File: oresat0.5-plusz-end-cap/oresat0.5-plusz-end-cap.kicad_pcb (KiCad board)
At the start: 2 copper layers, 105.6 x 105.6 mm, 44 parts, among them J2 U.FL-R-SMA, U1 LTC4305, U2 MMC5883MA, U3 MMC5883MA

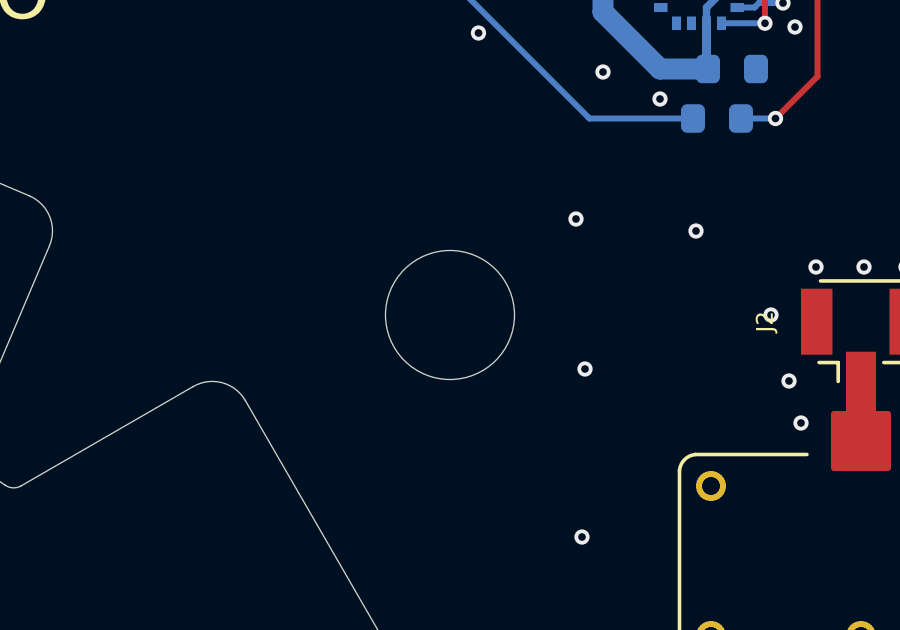
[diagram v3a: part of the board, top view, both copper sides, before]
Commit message: Oresat0.5 +Z End Cap. Still some weird library issues, but skipping for now.
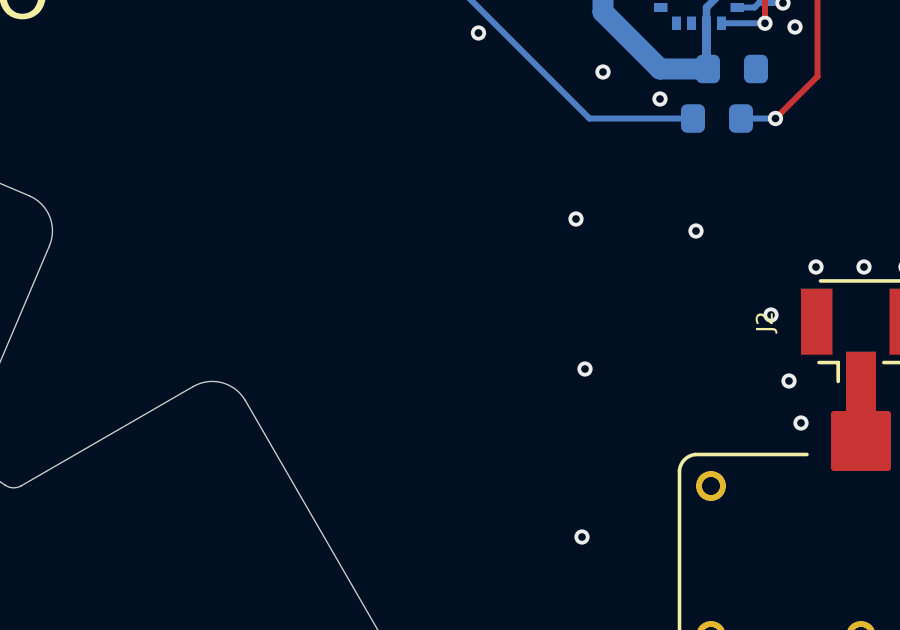
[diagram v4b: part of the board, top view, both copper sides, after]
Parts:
- removed REF**: MountingHole_4.3mm_M4, MountingHole:MountingHole_4.3mm_M4
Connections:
- U2 pad 12: (no net) -> unconnected-(U2-NC-Pad12)
- U2 pad 14: (no net) -> unconnected-(U2-NC-Pad14)
- U2 pad 3: (no net) -> unconnected-(U2-NC-Pad3)
- U2 pad 4: (no net) -> unconnected-(U2-NC-Pad4)
- U2 pad 5: (no net) -> unconnected-(U2-NC-Pad5)
- U2 pad 6: (no net) -> unconnected-(U2-NC-Pad6)
- U2 pad 7: (no net) -> unconnected-(U2-NC-Pad7)
- U2 pad 8: (no net) -> unconnected-(U2-NC-Pad8)
- U3 pad 12: (no net) -> unconnected-(U3-NC-Pad12)
- U3 pad 14: (no net) -> unconnected-(U3-NC-Pad14)
- U3 pad 3: (no net) -> unconnected-(U3-NC-Pad3)
- U3 pad 4: (no net) -> unconnected-(U3-NC-Pad4)
- U3 pad 5: (no net) -> unconnected-(U3-NC-Pad5)
- U3 pad 6: (no net) -> unconnected-(U3-NC-Pad6)
- U3 pad 7: (no net) -> unconnected-(U3-NC-Pad7)
- U3 pad 8: (no net) -> unconnected-(U3-NC-Pad8)
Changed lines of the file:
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@@
     (pad_to_mask_clearance 0)
     (pcbplotparams
-      (layerselection 0x0001000_7ffffffe)
+      (layerselection 0x00010fc_ffffffff)
       (plot_on_all_layers_selection 0x0000000_00000000)
       (disableapertmacros false)
@@
       (usegerberattributes true)
       (usegerberadvancedattributes true)
-      (creategerberjobfile true)
+      (creategerberjobfile false)
       (dashed_line_dash_ratio 12.000000)
       (dashed_line_gap_ratio 3.000000)
@@
       (drillshape 0)
       (scaleselection 1)
-      (outputdirectory "")
+      (outputdirectory "build")
     )
   )
@@
   (net 22 "unconnected-(J1-Pad12)")
   (net 23 "Net-(U2-INT)")
+  (net 24 "unconnected-(U2-NC-Pad3)")
+  (net 25 "unconnected-(U2-NC-Pad4)")
+  (net 26 "unconnected-(U2-NC-Pad5)")
+  (net 27 "unconnected-(U2-NC-Pad6)")
+  (net 28 "unconnected-(U2-NC-Pad7)")
+  (net 29 "unconnected-(U2-NC-Pad8)")
+  (net 30 "unconnected-(U2-NC-Pad12)")
+  (net 31 "unconnected-(U2-NC-Pad14)")
+  (net 32 "unconnected-(U3-NC-Pad3)")
+  (net 33 "unconnected-(U3-NC-Pad4)")
+  (net 34 "unconnected-(U3-NC-Pad5)")
+  (net 35 "unconnected-(U3-NC-Pad6)")
+  (net 36 "unconnected-(U3-NC-Pad7)")
+  (net 37 "unconnected-(U3-NC-Pad8)")
+  (net 38 "unconnected-(U3-NC-Pad12)")
+  (net 39 "unconnected-(U3-NC-Pad14)")
   (footprint "Connector_Coaxial:U.FL_Hirose_U.FL-R-SMT-1_Vertical" (layer "F.Cu")
     (at 191.9 78.7 90)
@@
       (net 6 "/MAG-SDA") (pinfunction "1") (pintype "passive"))
   )
-  (footprint "MountingHole:MountingHole_4.3mm_M4" (layer "F.Cu")
-    (at 178.2 78)
-    (descr "Mounting Hole 4.3mm, no annular, M4")
-    (tags "mounting hole 4.3mm no annular m4")
-    (attr exclude_from_pos_files exclude_from_bom)
-    (fp_text reference "REF**" (at 0 -5.3) (layer "F.SilkS") hide
-        (effects (font (size 0.56 0.56) (thickness 0.12)))
-    )
-    (fp_text value "MountingHole_4.3mm_M4" (at 0 5.3) (layer "F.Fab")
-        (effects (font (size 1 1) (thickness 0.15)))
-    )
-    (fp_text user "${REFERENCE}" (at 0 0) (layer "F.Fab")
-        (effects (font (size 1 1) (thickness 0.15)))
-    )
-    (fp_circle (center 0 0) (end 4.3 0)
-      (stroke (width 0.15) (type solid)) (fill none) (layer "Cmts.User"))
-    (fp_circle (center 0 0) (end 4.55 0)
-      (stroke (width 0.05) (type solid)) (fill none) (layer "F.CrtYd"))
-    (pad "" np_thru_hole circle (at 0 0) (size 4.3 4.3) (drill 4.3) (layers "*.Cu" "*.Mask"))
-  )
   (footprint "MountingHole:MountingHole_2.1mm" (layer "F.Cu")
     (at 121 154.5)
@@
       (net 1 "3.3V") (pinfunction "VDD") (pintype "power_in") (solder_mask_margin 0.0635))
     (pad "3" smd rect (at -0.25 1.275 90) (size 0.3 0.45) (layers "B.Cu" "B.Paste" "B.Mask")
-      (pinfunction "NC") (pintype "no_connect") (solder_mask_margin 0.0635))
+      (net 32 "unconnected-(U3-NC-Pad3)") (pinfunction "NC") (pintype "no_connect") (solder_mask_margin 0.0635))
     (pad "4" smd rect (at -0.75 1.275 90) (size 0.3 0.45) (layers "B.Cu" "B.Paste" "B.Mask")
-      (pinfunction "NC") (pintype "no_connect") (solder_mask_margin 0.0635))
+      (net 33 "unconnected-(U3-NC-Pad4)") (pinfunction "NC") (pintype "no_connect") (solder_mask_margin 0.0635))
     (pad "5" smd rect (at -1.275 0.75) (size 0.3 0.45) (layers "B.Cu" "B.Paste" "B.Mask")
-      (pinfunction "NC") (pintype "no_connect") (solder_mask_margin 0.0635))
+      (net 34 "unconnected-(U3-NC-Pad5)") (pinfunction "NC") (pintype "no_connect") (solder_mask_margin 0.0635))
     (pad "6" smd rect (at -1.275 0.25) (size 0.3 0.45) (layers "B.Cu" "B.Paste" "B.Mask")
-      (pinfunction "NC") (pintype "no_connect") (solder_mask_margin 0.0635))
+      (net 35 "unconnected-(U3-NC-Pad6)") (pinfunction "NC") (pintype "no_connect") (solder_mask_margin 0.0635))
     (pad "7" smd rect (at -1.275 -0.25) (size 0.3 0.45) (layers "B.Cu" "B.Paste" "B.Mask")
-      (pinfunction "NC") (pintype "no_connect") (solder_mask_margin 0.0635))
+      (net 36 "unconnected-(U3-NC-Pad7)") (pinfunction "NC") (pintype "no_connect") (solder_mask_margin 0.0635))
     (pad "8" smd rect (at -1.275 -0.75) (size 0.3 0.45) (layers "B.Cu" "B.Paste" "B.Mask")
-      (pinfunction "NC") (pintype "no_connect") (solder_mask_margin 0.0635))
+      (net 37 "unconnected-(U3-NC-Pad8)") (pinfunction "NC") (pintype "no_connect") (solder_mask_margin 0.0635))
     (pad "9" smd rect (at -0.75 -1.275 270) (size 0.3 0.45) (layers "B.Cu" "B.Paste" "B.Mask")
       (net 2 "GND") (pinfunction "GND") (pintype "power_in") (solder_mask_margin 0.0635))
@@
       (net 2 "GND") (pinfunction "GND") (pintype "power_in") (solder_mask_margin 0.0635))
     (pad "12" smd rect (at 0.75 -1.275 270) (size 0.3 0.45) (layers "B.Cu" "B.Paste" "B.Mask")
-      (pinfunction "NC") (pintype "no_connect") (solder_mask_margin 0.0635))
+      (net 38 "unconnected-(U3-NC-Pad12)") (pinfunction "NC") (pintype "no_connect") (solder_mask_margin 0.0635))
     (pad "13" smd rect (at 1.275 -0.75 180) (size 0.3 0.45) (layers "B.Cu" "B.Paste" "B.Mask")
       (net 1 "3.3V") (pinfunction "VDDIO") (pintype "power_in") (solder_mask_margin 0.0635))
     (pad "14" smd rect (at 1.275 -0.25 180) (size 0.3 0.45) (layers "B.Cu" "B.Paste" "B.Mask")
-      (pinfunction "NC") (pintype "no_connect") (solder_mask_margin 0.0635))
+      (net 39 "unconnected-(U3-NC-Pad14)") (pinfunction "NC") (pintype "no_connect") (solder_mask_margin 0.0635))
     (pad "15" smd rect (at 1.275 0.25 180) (size 0.3 0.45) (layers "B.Cu" "B.Paste" "B.Mask")
       (net 21 "Net-(U3-INT)") (pinfunction "INT") (pintype "output") (solder_mask_margin 0.0635))
@@
       (net 1 "3.3V") (pinfunction "VDD") (pintype "power_in") (solder_mask_margin 0.0635))
     (pad "3" smd rect (at -0.25 1.275) (size 0.3 0.45) (layers "B.Cu" "B.Paste" "B.Mask")
-      (pinfunction "NC") (pintype "no_connect") (solder_mask_margin 0.0635))
+      (net 24 "unconnected-(U2-NC-Pad3)") (pinfunction "NC") (pintype "no_connect") (solder_mask_margin 0.0635))
     (pad "4" smd rect (at -0.75 1.275) (size 0.3 0.45) (layers "B.Cu" "B.Paste" "B.Mask")
-      (pinfunction "NC") (pintype "no_connect") (solder_mask_margin 0.0635))
+      (net 25 "unconnected-(U2-NC-Pad4)") (pinfunction "NC") (pintype "no_connect") (solder_mask_margin 0.0635))
     (pad "5" smd rect (at -1.275 0.75 270) (size 0.3 0.45) (layers "B.Cu" "B.Paste" "B.Mask")
-      (pinfunction "NC") (pintype "no_connect") (solder_mask_margin 0.0635))
+      (net 26 "unconnected-(U2-NC-Pad5)") (pinfunction "NC") (pintype "no_connect") (solder_mask_margin 0.0635))
     (pad "6" smd rect (at -1.275 0.25 270) (size 0.3 0.45) (layers "B.Cu" "B.Paste" "B.Mask")
-      (pinfunction "NC") (pintype "no_connect") (solder_mask_margin 0.0635))
+      (net 27 "unconnected-(U2-NC-Pad6)") (pinfunction "NC") (pintype "no_connect") (solder_mask_margin 0.0635))
     (pad "7" smd rect (at -1.275 -0.25 270) (size 0.3 0.45) (layers "B.Cu" "B.Paste" "B.Mask")
-      (pinfunction "NC") (pintype "no_connect") (solder_mask_margin 0.0635))
+      (net 28 "unconnected-(U2-NC-Pad7)") (pinfunction "NC") (pintype "no_connect") (solder_mask_margin 0.0635))
     (pad "8" smd rect (at -1.275 -0.75 270) (size 0.3 0.45) (layers "B.Cu" "B.Paste" "B.Mask")
-      (pinfunction "NC") (pintype "no_connect") (solder_mask_margin 0.0635))
+      (net 29 "unconnected-(U2-NC-Pad8)") (pinfunction "NC") (pintype "no_connect") (solder_mask_margin 0.0635))
     (pad "9" smd rect (at -0.75 -1.275 180) (size 0.3 0.45) (layers "B.Cu" "B.Paste" "B.Mask")
       (net 2 "GND") (pinfunction "GND") (pintype "power_in") (solder_mask_margin 0.0635))
@@
       (net 2 "GND") (pinfunction "GND") (pintype "power_in") (solder_mask_margin 0.0635))
     (pad "12" smd rect (at 0.75 -1.275 180) (size 0.3 0.45) (layers "B.Cu" "B.Paste" "B.Mask")
-      (pinfunction "NC") (pintype "no_connect") (solder_mask_margin 0.0635))
+      (net 30 "unconnected-(U2-NC-Pad12)") (pinfunction "NC") (pintype "no_connect") (solder_mask_margin 0.0635))
     (pad "13" smd rect (at 1.275 -0.75 90) (size 0.3 0.45) (layers "B.Cu" "B.Paste" "B.Mask")
       (net 1 "3.3V") (pinfunction "VDDIO") (pintype "power_in") (solder_mask_margin 0.0635))
     (pad "14" smd rect (at 1.275 -0.25 90) (size 0.3 0.45) (layers "B.Cu" "B.Paste" "B.Mask")
-      (pinfunction "NC") (pintype "no_connect") (solder_mask_margin 0.0635))
+      (net 31 "unconnected-(U2-NC-Pad14)") (pinfunction "NC") (pintype "no_connect") (solder_mask_margin 0.0635))
     (pad "15" smd rect (at 1.275 0.25 90) (size 0.3 0.45) (layers "B.Cu" "B.Paste" "B.Mask")
       (net 23 "Net-(U2-INT)") (pinfunction "INT") (pintype "output") (solder_mask_margin 0.0635))

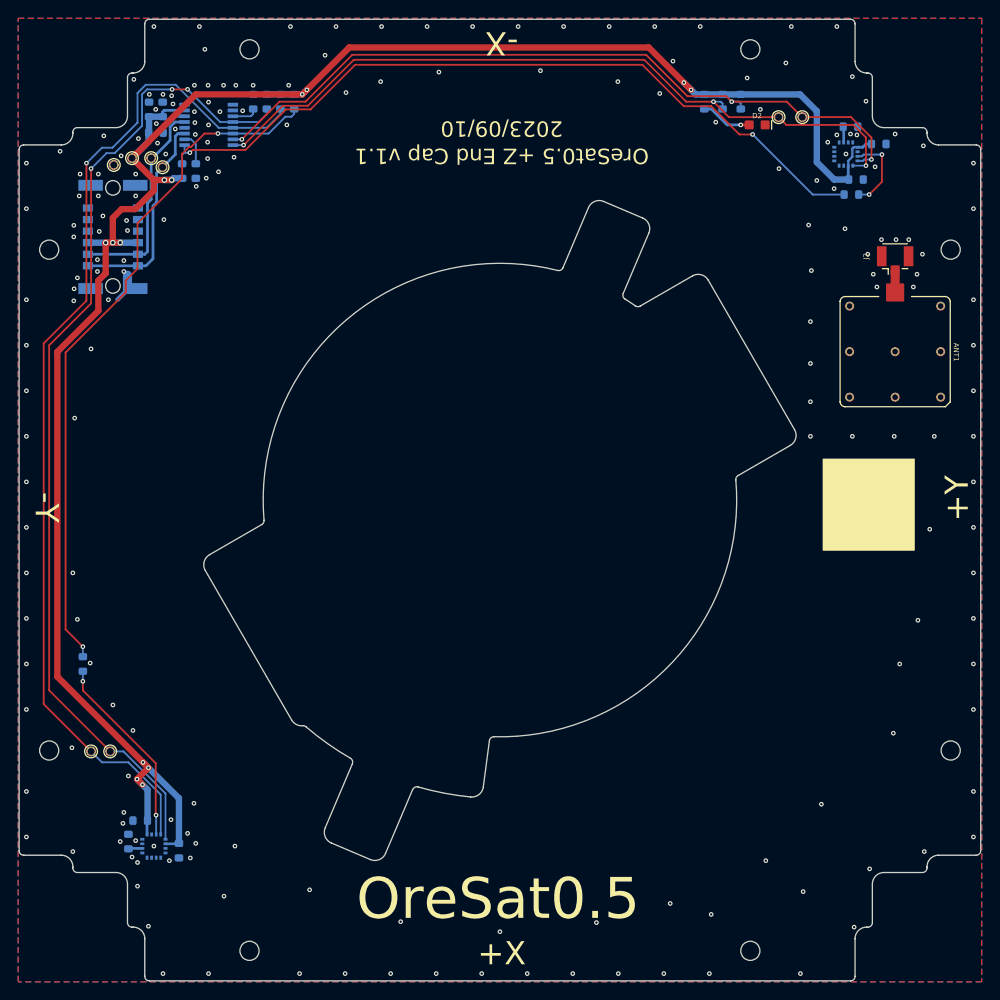
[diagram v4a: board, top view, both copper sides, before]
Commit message: Upgrades OreSat0.5 +Z End Cap to v1.2 -- fits the new deployer, and cleans up a bunch of library issues.
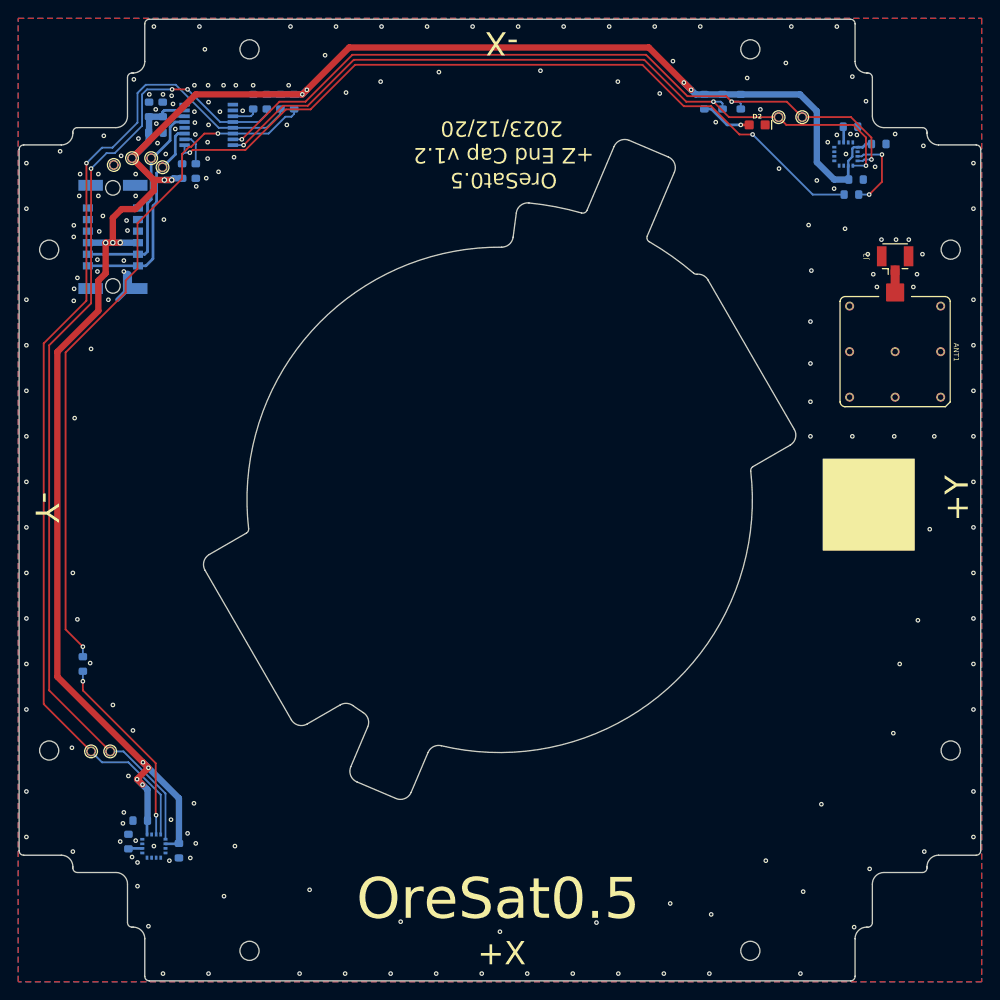
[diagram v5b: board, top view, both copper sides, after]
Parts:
- D2: footprint oresat0-plusz-end-cap:LED-0603 -> oresat0.5-plusz-end-cap:LED-0603
- U1: footprint oresat0-plusz-end-cap:16-SSOP -> oresat0.5-plusz-end-cap:16-SSOP
- U2, U3: footprint oresat0-plusz-end-cap:LGA-16(3X3) -> oresat0.5-plusz-end-cap:LGA-16(3X3)
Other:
- outline, holes or cut-outs redrawn
- board text added: "2023/12/20"
- board text added: "OreSat0.5 +Z End Cap v1.2"
- board text removed: "2023/09/10"
- board text removed: "OreSat0.5 +Z End Cap v1.1"

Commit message: corrected board outline for OreSat 0.5 +z endcap
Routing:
- net GND: vias 198 -> 183
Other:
- outline, holes or cut-outs redrawn

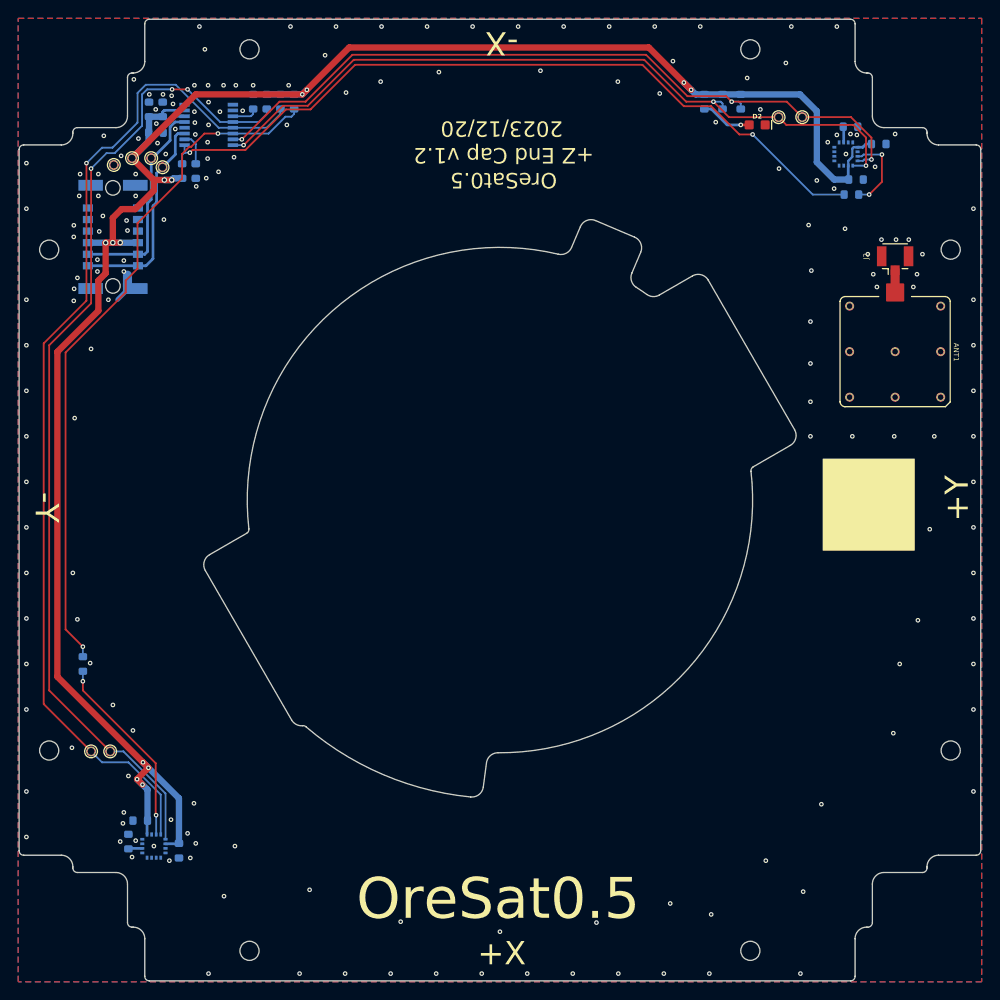
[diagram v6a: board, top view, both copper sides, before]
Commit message: updated mmc5883 magnetometer to mmc5983 for both OreSat 0.5 +Z and -Z endcaps
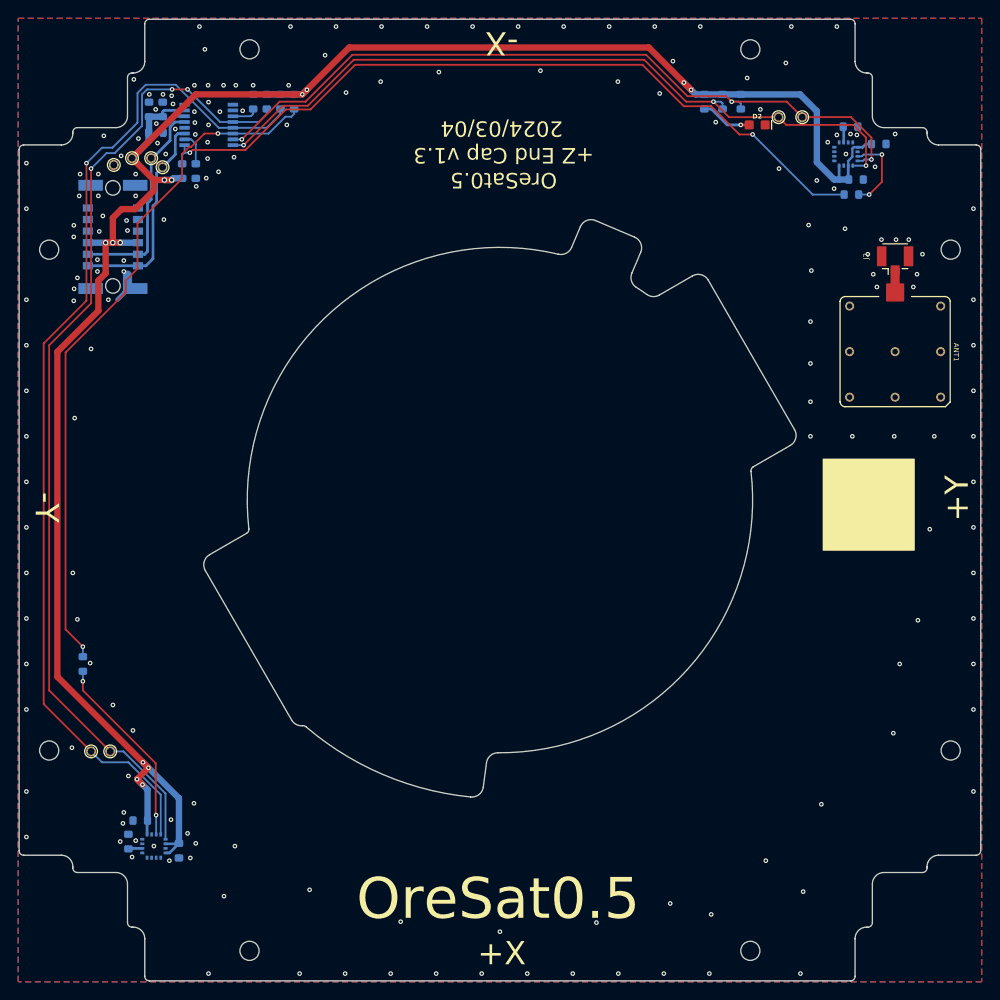
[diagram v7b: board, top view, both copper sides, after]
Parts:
- C1, C10, C12, C13, C2, C3, C4, C7, D2, J1, R1, R10, R2, R3, R4, R5, R6, R7, R8, R9: value (none) -> ~
- U2, U3: value MMC5883MA -> MMC5983MA; footprint oresat0.5-plusz-end-cap:LGA-16(3X3) -> oresat-ics:LGA-16(3X3)
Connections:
- U2 pad 4: unconnected-(U2-NC-Pad4) -> 3.3V
- U3 pad 4: unconnected-(U3-NC-Pad4) -> 3.3V
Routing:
- net 3.3V: track 223.8 -> 227.3 mm
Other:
- board text added: "2024/03/04"
- board text added: "OreSat0.5 +Z End Cap v1.3"
- board text removed: "2023/12/20"
- board text removed: "OreSat0.5 +Z End Cap v1.2"
